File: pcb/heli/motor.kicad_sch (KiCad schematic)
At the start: 7 parts, among them M1 Motor_DC, Q2 BC547, Q3 IRLZ44N

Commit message: 
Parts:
- D2: DIGIKEY https://www.digikey.de/en/products/detail/smc-diode-solutio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 -> 1655-1N5819WCT-ND
- M1: DIGIKEY https://www.digikey.de/en/products/detail/adam-tech/PH1-10-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 -> 2057-PH1-10-UA-ND
- R10: DIGIKEY https://www.digikey.de/en/products/detail/walsin-technology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 -> 1292-WR06X103JTLCT-ND
- R8: DIGIKEY https://www.digikey.de/en/products/detail/walsin-technology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 -> 1292-WR06X105JTLCT-ND
- R9: DIGIKEY https://www.digikey.de/en/products/detail/stackpole-electro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 -> RMCF0603JT20K0CT-ND
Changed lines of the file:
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@@
       (effects (font (size 1.27 1.27)) hide)
     )
-    (property "DIGIKEY" "https://www.digikey.de/en/products/detail/walsin-technology-corporation/WR06X105-JTL/13239221" (id 4) (at 34.29 62.23 0)
+    (property "DIGIKEY" "1292-WR06X105JTLCT-ND" (id 4) (at 34.29 62.23 0)
       (effects (font (size 1.27 1.27)) hide)
     )
@@
       (effects (font (size 1.27 1.27)) hide)
     )
-    (property "DIGIKEY" "https://www.digikey.de/en/products/detail/smc-diode-solutions/1N5819W/15964237" (id 4) (at 68.58 44.45 0)
+    (property "DIGIKEY" "1655-1N5819WCT-ND" (id 4) (at 68.58 44.45 0)
       (effects (font (size 1.27 1.27)) hide)
     )
@@
       (effects (font (size 1.27 1.27)) hide)
     )
-    (property "DIGIKEY" "https://www.digikey.de/en/products/detail/stackpole-electronics-inc/RMCF0603JT20K0/1758001" (id 4) (at 43.18 68.58 0)
+    (property "DIGIKEY" "RMCF0603JT20K0CT-ND" (id 4) (at 43.18 68.58 0)
       (effects (font (size 1.27 1.27)) hide)
     )
@@
       (effects (font (size 1.27 1.27)) hide)
     )
-    (property "DIGIKEY" "https://www.digikey.de/en/products/detail/walsin-technology-corporation/WR06X103-JTL/13239132" (id 4) (at 54.61 53.34 0)
+    (property "DIGIKEY" "1292-WR06X103JTLCT-ND" (id 4) (at 54.61 53.34 0)
       (effects (font (size 1.27 1.27)) hide)
     )
@@
       (effects (font (size 1.27 1.27)) hide)
     )
-    (property "DIGIKEY" "https://www.digikey.de/en/products/detail/adam-tech/PH1-10-UA/9830653" (id 4) (at 76.2 43.18 0)
+    (property "DIGIKEY" "2057-PH1-10-UA-ND" (id 4) (at 76.2 43.18 0)
       (effects (font (size 1.27 1.27)) hide)
     )

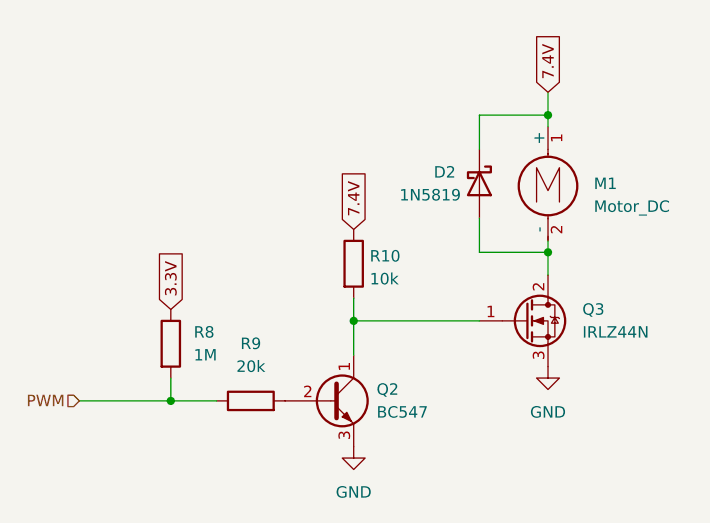
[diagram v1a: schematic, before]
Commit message: 
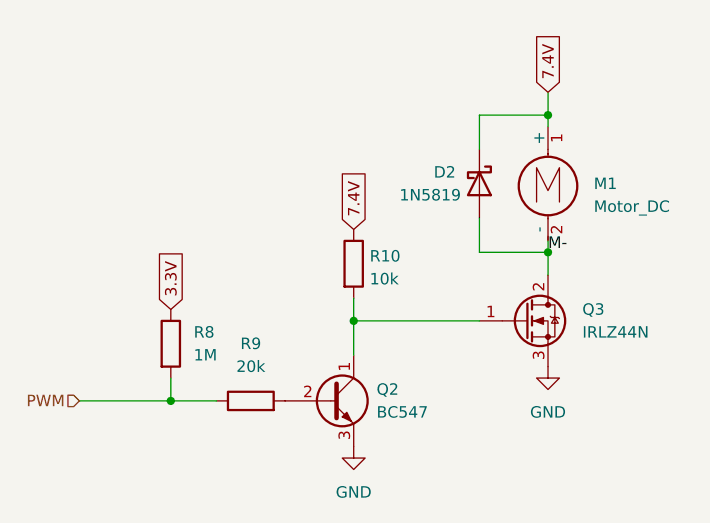
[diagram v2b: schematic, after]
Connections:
- net M-: now reaches D2.2 (A), M1.2 (-), Q3.2 (D)
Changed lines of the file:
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@@
     (stroke (width 0) (type default) (color 0 0 0 0))
+  )
+  (label "M-" (at 76.2 52.07 0)
+    (effects (font (size 1.27 1.27)) (justify left bottom))
   )
   (global_label "7.4V" (shape input) (at 54.61 49.53 90) (fields_autoplaced)
